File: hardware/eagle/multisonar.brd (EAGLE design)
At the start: 99 x 99 mm, 25 parts, among them IC1 ATMEGA328-20P, J1 ARDUINO_R3_SHIELDUNO_R3_SHIEL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, Y1 16MHZ

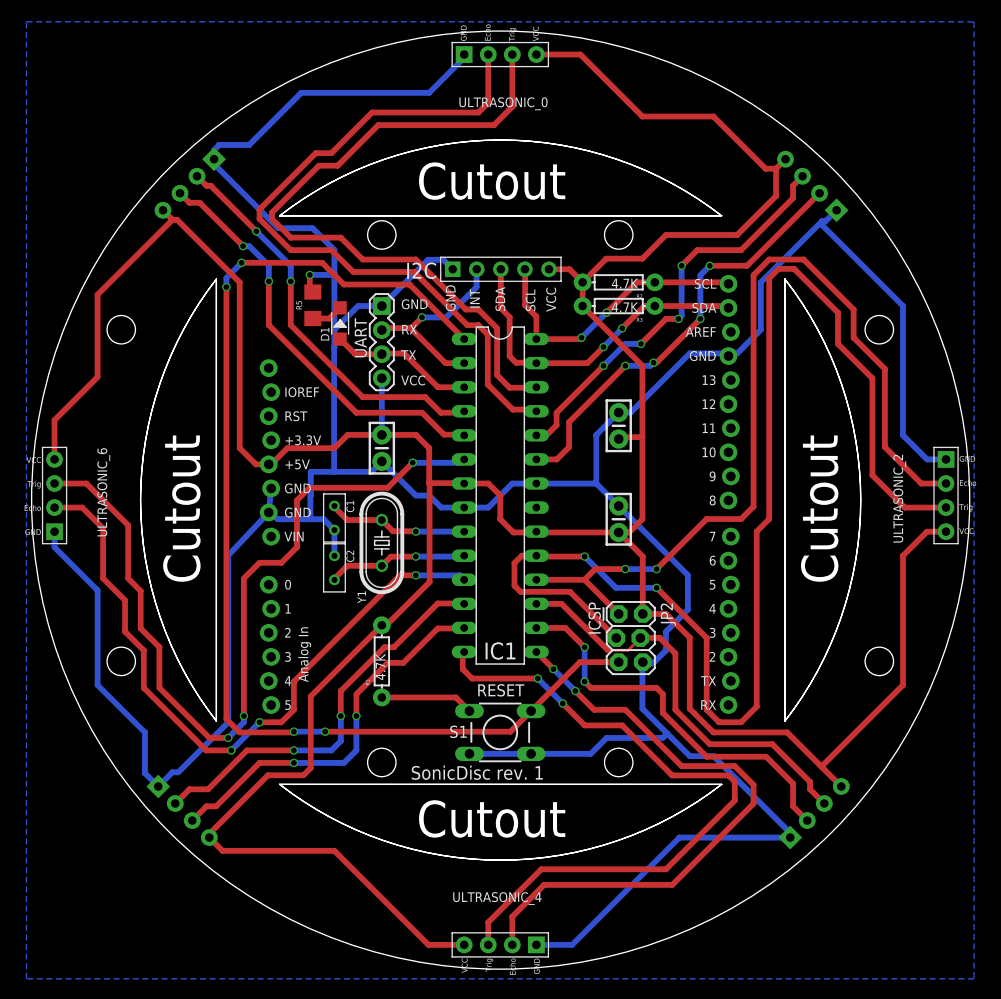
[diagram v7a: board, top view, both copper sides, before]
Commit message: Add rev. 2 board
* Move I2C header down for easier cabling through the cutout
* Add OSH logo
* Add PCBWay.com logo (sponsors)
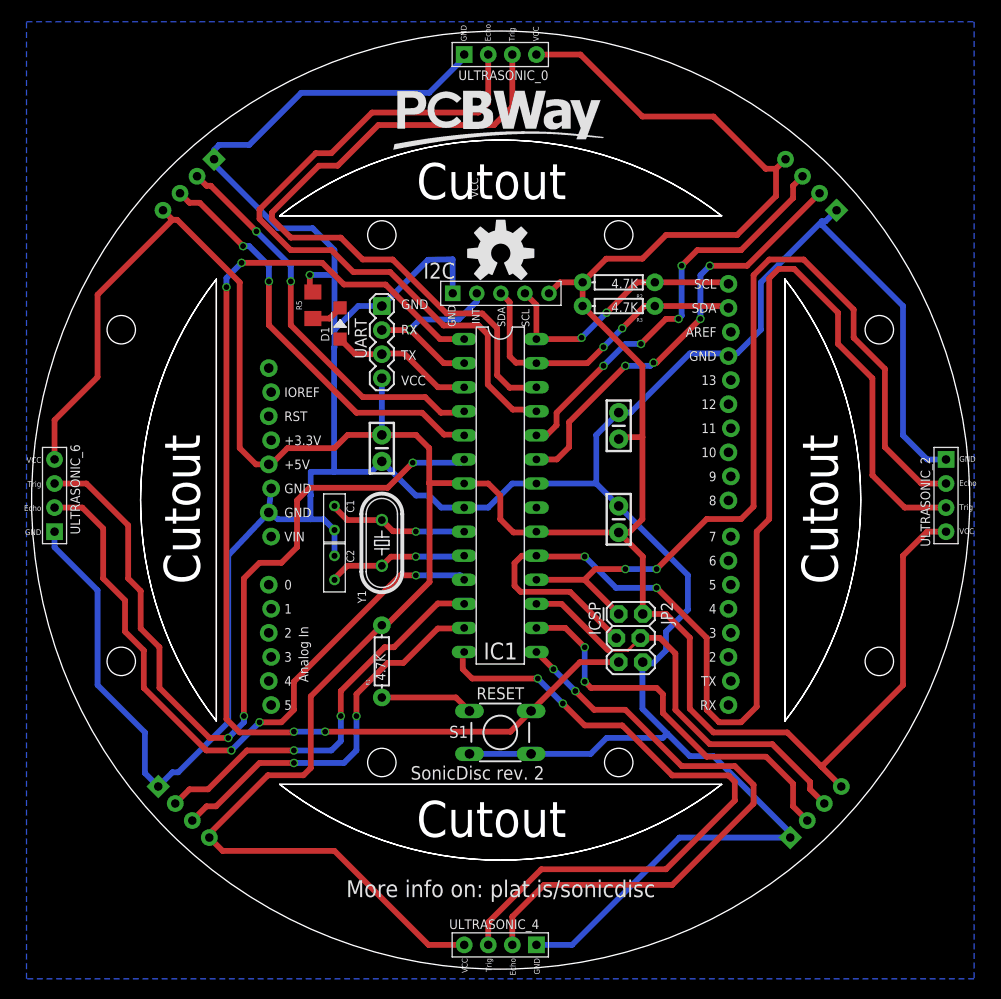
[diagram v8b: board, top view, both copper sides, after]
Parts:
- added U$1: (no value), SparkFun-Aesthetics:OSHW-LOGO-L
- moved I2C 2.54 mm to (82.6, 71.3)
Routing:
- net GND: track 391.1 -> 394.3 mm
- net SDA: track 35.6 -> 33.0 mm
- net SCL: track 30.7 -> 28.1 mm
- net RX/INT: track 21.0 -> 19.3 mm
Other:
- board text added: "More info on: plat.is/sonicdisc"
- board text added: "SonicDisc rev. 2"
- board text removed: "SonicDisc rev. 1"
